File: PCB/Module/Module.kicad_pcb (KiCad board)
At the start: 2 copper layers, 80.1 x 42.7 mm, 17 parts

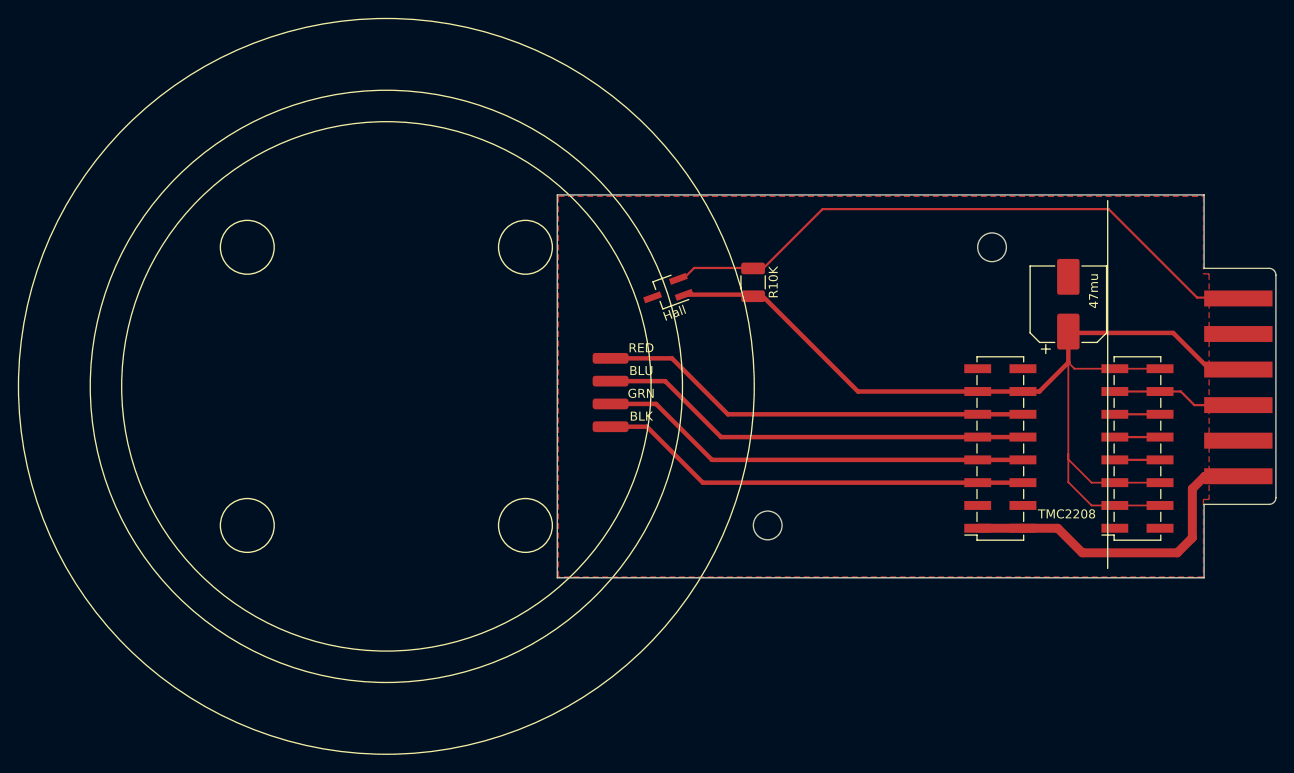
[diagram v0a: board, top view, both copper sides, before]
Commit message: rename module PCB files from SplitFlap.kicad to Module.kicad
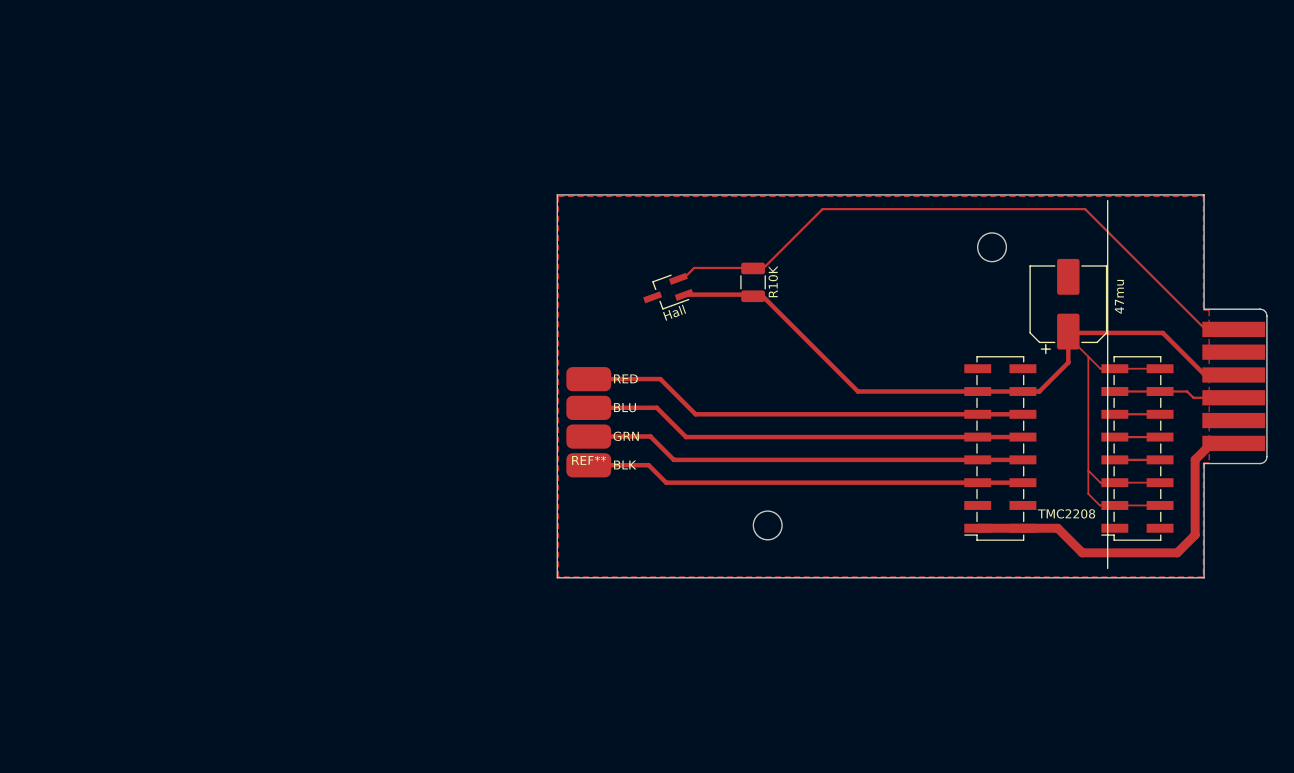
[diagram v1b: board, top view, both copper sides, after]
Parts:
- removed BLK, BLU, GRN, RED: SolderWirePad_1x01_SMD_1x2mm, Connector_Wire:SolderWirePad_1x01_SMD_1x2mm
- added REF**: AVX-00-9176-004-873-X06, Jumper:AVX-00-9176-004-873-X06, F.Cu at (119.1, 97.6)
- moved ? 2.53 mm to (191.6, 96.3)
- moved ? 2.34 mm to (191.5, 81.4)
- moved ? 2.30 mm to (191.0, 92.6)
- moved ? 2.09 mm to (191.0, 85.0)
- moved ? 0.97 mm to (191.0, 90.1)
- moved ? 0.79 mm to (191.0, 87.5)
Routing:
- net +5V: track 116.7 -> 110.6 mm
- net +12V: track 33.6 -> 37.2 mm
- net A2: track 48.4 -> 50.0 mm
- net A1: track 48.4 -> 49.7 mm
- net B1: track 48.4 -> 49.5 mm
- net Step: track 14.4 -> 13.5 mm
- net B2: track 48.4 -> 49.2 mm
- net Hall: track 65.0 -> 65.8 mm
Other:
- board size 80.1 x 42.7 mm -> 79.1 x 42.7 mm
- board text added: "BLK"
- board text added: "BLU"
- board text added: "GRN"
- board text added: "RED"

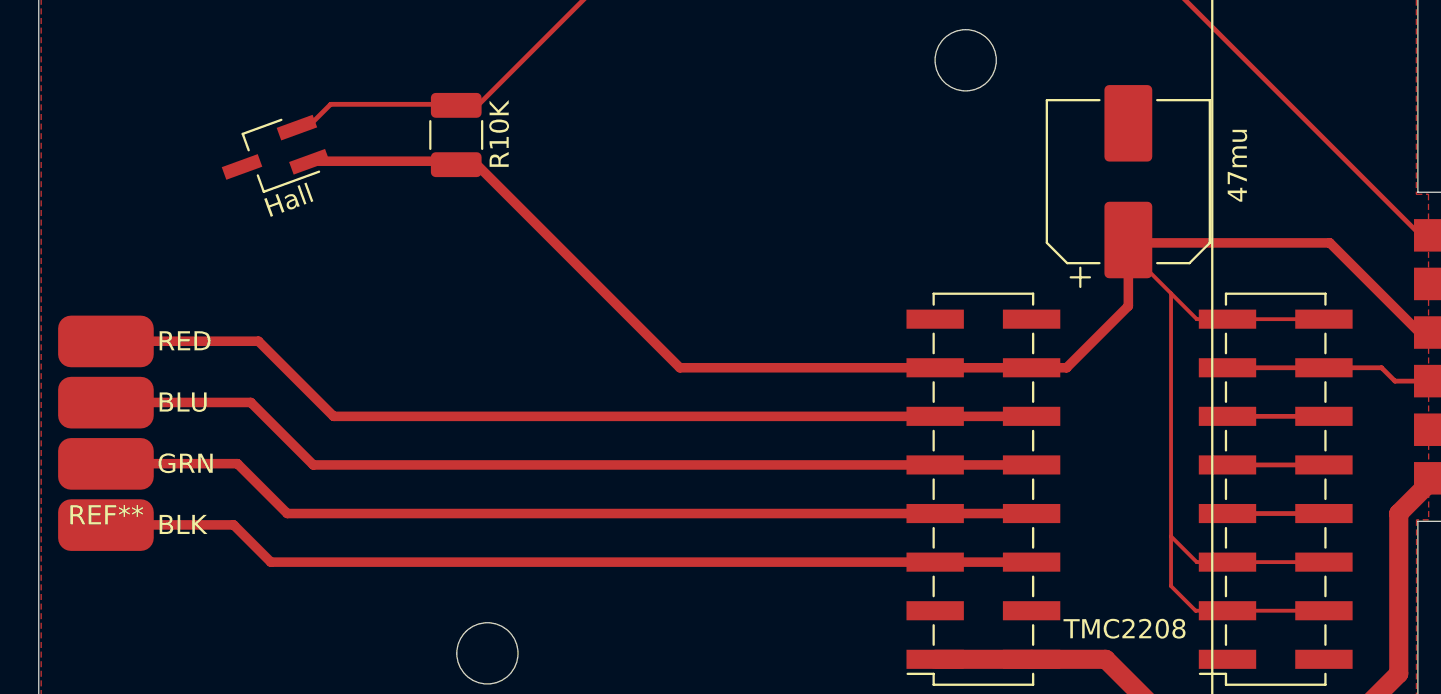
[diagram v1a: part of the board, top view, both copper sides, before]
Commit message: update PCB to newest version, remove obsolete files
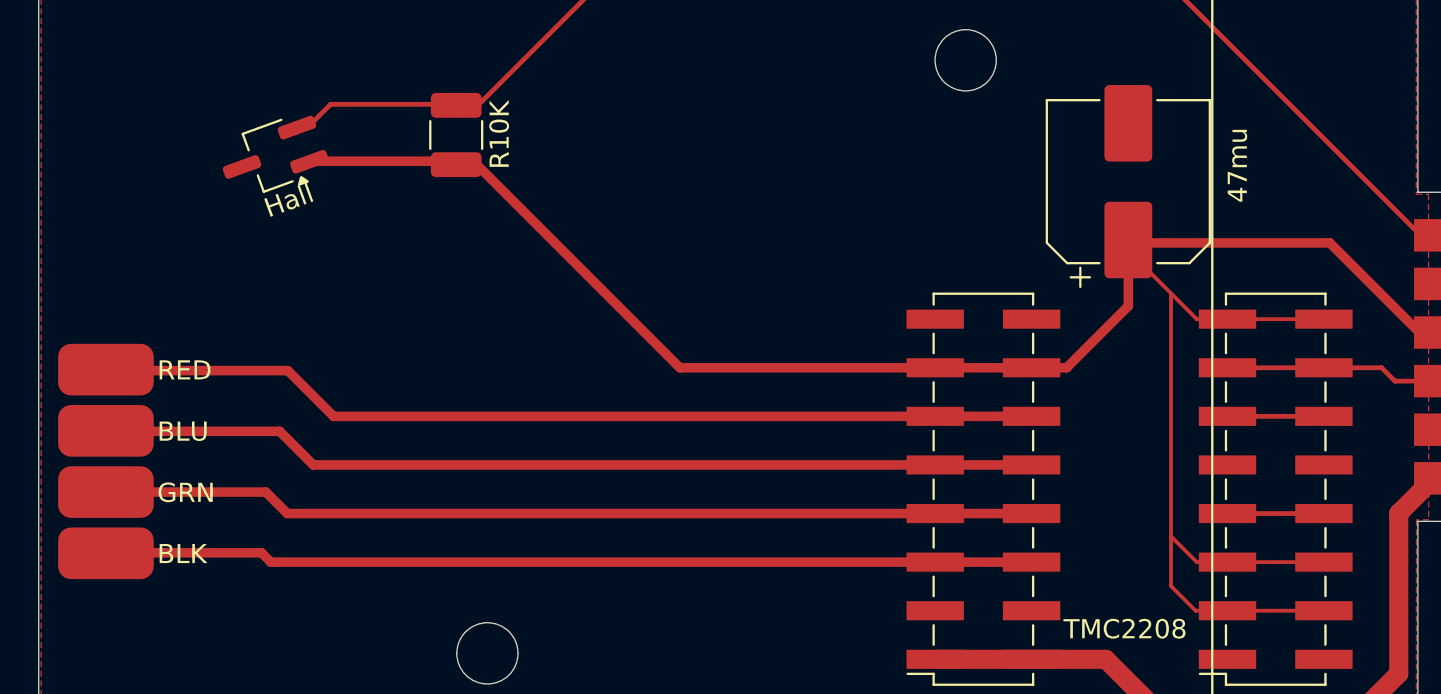
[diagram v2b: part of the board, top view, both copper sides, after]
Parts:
- REF**: footprint Jumper:AVX-00-9176-004-873-X06 -> Custom_Footprints:AVX-00-9176-004-873-X06
- moved REF** 1.47 mm to (119.1, 99.1)
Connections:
- REF** pad : B2 -> (no net)
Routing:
- net PDN: track 5.04 -> 0.00 mm
- net A2: track 50.0 -> 47.8 mm
- net A1: track 49.7 -> 47.6 mm
- net B1: track 49.5 -> 47.4 mm
- net B2: track 49.2 -> 47.1 mm
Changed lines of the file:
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@@
 	(net 10 "NC")
 	(net 11 "Clock")
-	(net 12 "PDN")
 	(footprint ""
 		(layer "F.Cu")
@@
 		)
 		(fp_line
-			(start -2 -1.61)
+			(start -0.525 -1.61)
 			(end 1.075 -1.61)
 			(stroke
@@
 			(layer "F.SilkS")
 		)
+		(fp_poly
+			(pts
+				(xy -1.025 -1.56) (xy -1.265 -1.89) (xy -0.785 -1.89) (xy -1.025 -1.56)
+			)
+			(stroke
+				(width 0.12)
+				(type solid)
+			)
+			(fill yes)
+			(layer "F.SilkS")
+		)
 		(fp_line
 			(start 2.95 1.74)
@@
 			)
 		)
-		(pad "1" smd rect
+		(pad "1" smd roundrect
 			(at -1.7 -0.95 200)
 			(size 2 0.7)
 			(layers "F.Cu" "F.Mask" "F.Paste")
+			(roundrect_rratio 0.25)
 			(net 2 "+5V")
 		)
-		(pad "2" smd rect
+		(pad "2" smd roundrect
 			(at -1.7 0.95 200)
 			(size 2 0.7)
 			(layers "F.Cu" "F.Mask" "F.Paste")
+			(roundrect_rratio 0.25)
 			(net 3 "Hall")
 		)
-		(pad "3" smd rect
+		(pad "3" smd roundrect
 			(at 1.699999 0 200)
 			(size 2 0.7)
 			(layers "F.Cu" "F.Mask" "F.Paste")
+			(roundrect_rratio 0.25)
 			(net 1 "GND")
 		)
 		(embedded_fonts no)
-		(model "${KICAD6_3DMODEL_DIR}/Package_TO_SOT_SMD.3dshapes/SOT-23W_Handsoldering.wrl"
+		(model "${KICAD9_3DMODEL_DIR}/Package_TO_SOT_SMD.3dshapes/SOT-23W_Handsoldering.step"
 			(offset
 				(xyz 0 0 0)
@@
 		)
 	)
-	(footprint "Jumper:AVX-00-9176-004-873-X06"
+	(footprint "Custom_Footprints:AVX-00-9176-004-873-X06"
 		(layer "F.Cu")
-		(at 119.126 97.611)
+		(at 119.126 99.085)
 		(property "Reference" "REF**"
 			(at 0 -0.5 0)
 			(unlocked yes)
 			(layer "F.SilkS")
+			(hide yes)
 			(effects
 				(font
@@
 			(layers "F.Cu" "F.Mask" "F.Paste")
 			(roundrect_rratio 0.25)
-			(net 9 "A2")
 		)
 		(pad "" smd roundrect
@@
 			(layers "F.Cu" "F.Mask" "F.Paste")
 			(roundrect_rratio 0.25)
-			(net 8 "A1")
 		)
 		(pad "" smd roundrect
@@
 			(layers "F.Cu" "F.Mask" "F.Paste")
 			(roundrect_rratio 0.25)
-			(net 7 "B1")
 		)
 		(pad "" smd roundrect
@@
 			(layers "F.Cu" "F.Mask" "F.Paste")
 			(roundrect_rratio 0.25)
-			(net 6 "B2")
 		)
 		(embedded_fonts no)
-		(model "${KICAD9_FOOTPRINT_DIR}/Jumper.pretty/AVX-00-9176-004-873-X06.step"
+		(model "/Users/stefan/Documents/KiCad/Custom_Libraries/AVX-00-9176-004-873-X06.step"
 			(offset
 				(xyz 8.5 11.5 -6.5)
@@
 			(net 10 "NC")
 		)
-		(pad "9" smd rect
+		(pad "9 PDN" smd rect
 			(at 2.52 1.27 180)
 			(size 3 1)
 			(layers "F.Cu" "F.Mask" "F.Paste")
-			(net 12 "PDN")
+			(net 1 "GND")
 		)
-		(pad "10" smd rect
+		(pad "10 PDN" smd rect
 			(at -2.52 1.27 180)
 			(size 3 1)
 			(layers "F.Cu" "F.Mask" "F.Paste")
-			(net 12 "PDN")
+			(net 1 "GND")
 		)
 		(pad "11" smd rect
@@
 	)
 	(gr_text "RED"
-		(at 121.8 88.6 0)
+		(at 121.8 90.12 0)
 		(layer "F.SilkS")
 		(effects
@@
 	)
 	(gr_text "GRN"
-		(at 121.8 95 0)
+		(at 121.8 96.52 0)
 		(layer "F.SilkS")
 		(effects
@@
 	)
 	(gr_text "BLU"
-		(at 121.8 91.8 0)
+		(at 121.8 93.32 0)
 		(layer "F.SilkS")
 		(effects
@@
 	)
 	(gr_text "BLK"
-		(at 121.8 98.2 0)
+		(at 121.8 99.72 0)
 		(layer "F.SilkS")
 		(effects
@@
 	)
 	(segment
-		(start 125.8 97.6)
-		(end 119.137 97.6)
-		(width 0.5)
-		(layer "F.Cu")
-		(net 6)
-	)
-	(segment
 		(start 127.746727 99.546727)
-		(end 125.8 97.6)
+		(end 127.26 99.06)
 		(width 0.5)
 		(layer "F.Cu")
@@
 	)
 	(segment
-		(start 126 94.4)
-		(end 119.137 94.4)
+		(start 127.26 99.06)
+		(end 120.597 99.06)
 		(width 0.5)
 		(layer "F.Cu")
-		(net 7)
+		(net 6)
 	)
 	(segment
@@
 	(segment
 		(start 128.606727 97.006727)
-		(end 126 94.4)
+		(end 127.485 95.885)
 		(width 0.5)
 		(layer "F.Cu")
@@
 	)
 	(segment
-		(start 126.7 91.2)
-		(end 119.137 91.2)
+		(start 127.485 95.885)
+		(end 120.622 95.885)
+		(width 0.5)
+		(layer "F.Cu")
+		(net 7)
+	)
+	(segment
+		(start 128.21 92.71)
+		(end 120.647 92.71)
 		(width 0.5)
 		(layer "F.Cu")
@@
 	(segment
 		(start 129.966727 94.466727)
-		(end 126.7 91.2)
+		(end 128.21 92.71)
 		(width 0.5)
 		(layer "F.Cu")
@@
 	)
 	(segment
-		(start 162.471179 91.926727)
-		(end 131.026727 91.926727)
+		(start 128.635 89.535)
+		(end 120.672 89.535)
 		(width 0.5)
 		(layer "F.Cu")
@@
 	)
 	(segment
-		(start 131.026727 91.926727)
-		(end 127.1 88)
+		(start 162.471179 91.926727)
+		(end 167.511179 91.926727)
 		(width 0.5)
 		(layer "F.Cu")
@@
 	)
 	(segment
-		(start 127.1 88)
-		(end 119.137 88)
+		(start 162.471179 91.926727)
+		(end 131.026727 91.926727)
 		(width 0.5)
 		(layer "F.Cu")
@@
 	)
 	(segment
-		(start 162.471179 91.926727)
-		(end 167.511179 91.926727)
+		(start 131.026727 91.926727)
+		(end 128.635 89.535)
 		(width 0.5)
 		(layer "F.Cu")
@@
 		(net 11)
 	)
-	(segment
-		(start 177.751179 94.466727)
-		(end 182.791179 94.466727)
-		(width 0.25)
-		(layer "F.Cu")
-		(net 12)
-	)
 	(zone
